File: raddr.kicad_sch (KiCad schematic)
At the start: 8 parts, among them J1 Conn_01x03, J2 Conn_01x01, J3 Conn_01x04, J4 Conn_01x01, U1 PMS150C-U06

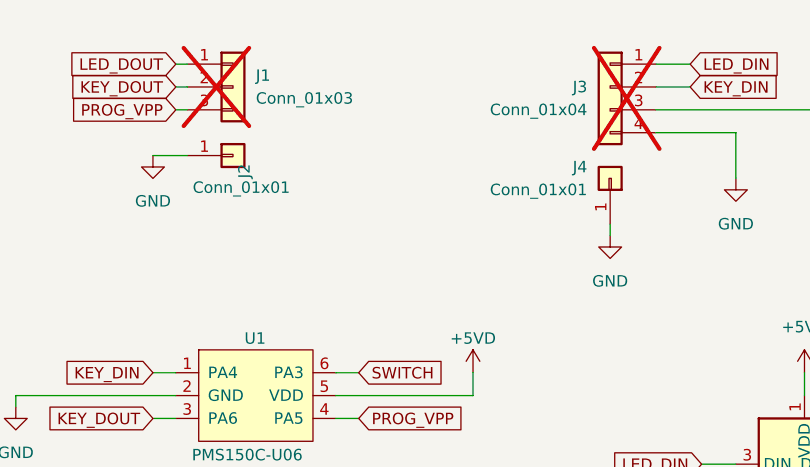
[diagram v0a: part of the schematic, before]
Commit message: Also mark single pins at the bottom as DNP
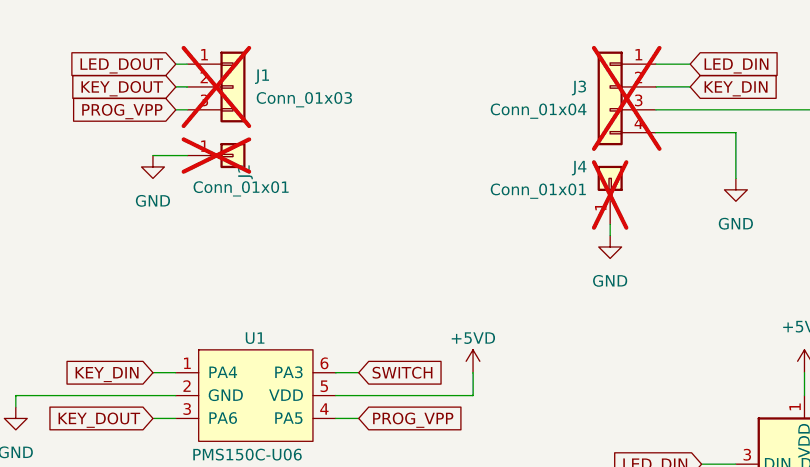
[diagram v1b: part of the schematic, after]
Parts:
- J2, J4: now not fitted
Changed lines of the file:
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@@
 		(in_bom yes)
 		(on_board yes)
-		(dnp no)
+		(dnp yes)
 		(property "Reference" "J2"
 			(at 95.2501 44.45 90)
@@
 		(in_bom yes)
 		(on_board yes)
-		(dnp no)
+		(dnp yes)
 		(fields_autoplaced yes)
 		(property "Reference" "J4"

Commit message: Redesign
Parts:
- removed CH1: choc_v1_SW_HS, PCM_marbastlib-choc:SW_choc_v1_HS_CPG135001S30_1u, symbol PCM_marbastlib-choc:choc_v1_SW_HS_CPG135001S30
- removed J1: Conn_01x03, Connector_PinSocket_2.54mm:PinSocket_1x03_P2.54mm_Vertical, symbol Connector_Generic:Conn_01x03
- removed J2, J4: Conn_01x01, Connector_PinSocket_2.54mm:PinSocket_1x01_P2.54mm_Vertical, symbol Connector_Generic:Conn_01x01
- removed U1: PMS150C-U06, Package_TO_SOT_SMD:SOT-23-6, symbol Padauk:PMS150C-U06
- added CH1: KS33_SW_HS, PCM_marbastlib-xp-gateron_lp:SW_KS33_HS_KS-2P02B01-02_HS_1u, symbol PCM_marbastlib-gateron_lp:KS33_SW_HS_KS-2P02B01-02
- added DBG1, OUT1: Conn_01x04, Connector_PinSocket_2.54mm:PinSocket_1x04_P2.54mm_Vertical, symbol Connector_Generic:Conn_01x04
- added U1: PY32F002AL1xS, Package_SO:SOP-8_3.9x4.9mm_P1.27mm, symbol MCU_Puya:PY32F002AL1xS
- renumbered J3 to IN1
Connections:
- net +5VD: now also DBG1.3 (Pin_3), OUT1.3 (Pin_3), U1.1 (VCC)
- net GND: now also CH1.2, DBG1.4 (Pin_4), OUT1.4 (Pin_4), U1.8 (GND)
- net KEY_DIN: now also U1.3 (PA3)
- net KEY_DOUT: now also OUT1.2 (Pin_2), U1.2 (PA4/PA10)
- net LED_DOUT: now also OUT1.1 (Pin_1)
- net SWITCH: now also CH1.1, U1.7 (PA1)
- new net SWC: DBG1.1 (Pin_1), U1.4 (PA14/SWCLK/PB3)
- new net SWD: DBG1.2 (Pin_2), U1.5 (PA13/SWDIO)
